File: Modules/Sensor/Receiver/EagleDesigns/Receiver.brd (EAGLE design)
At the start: 100 x 80 mm, 11 parts, among them U2 ATMEGA328P_TQFP

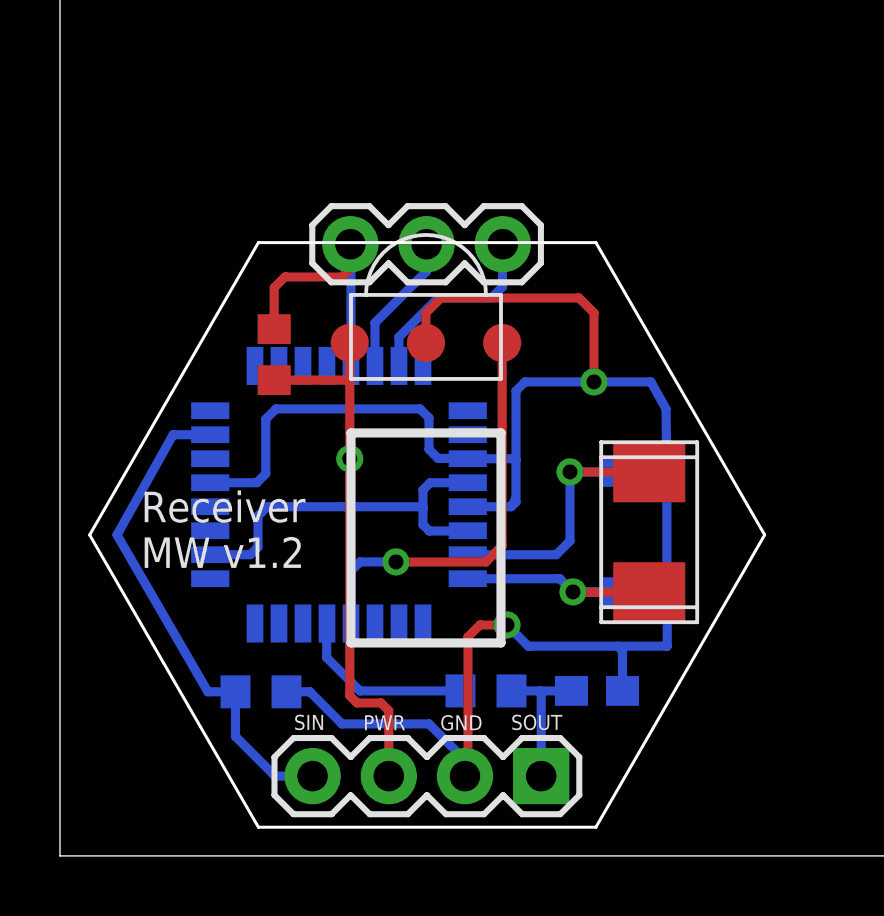
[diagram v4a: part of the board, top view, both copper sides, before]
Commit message: Receiver: removed crystal, modified to work with new bootloader #29
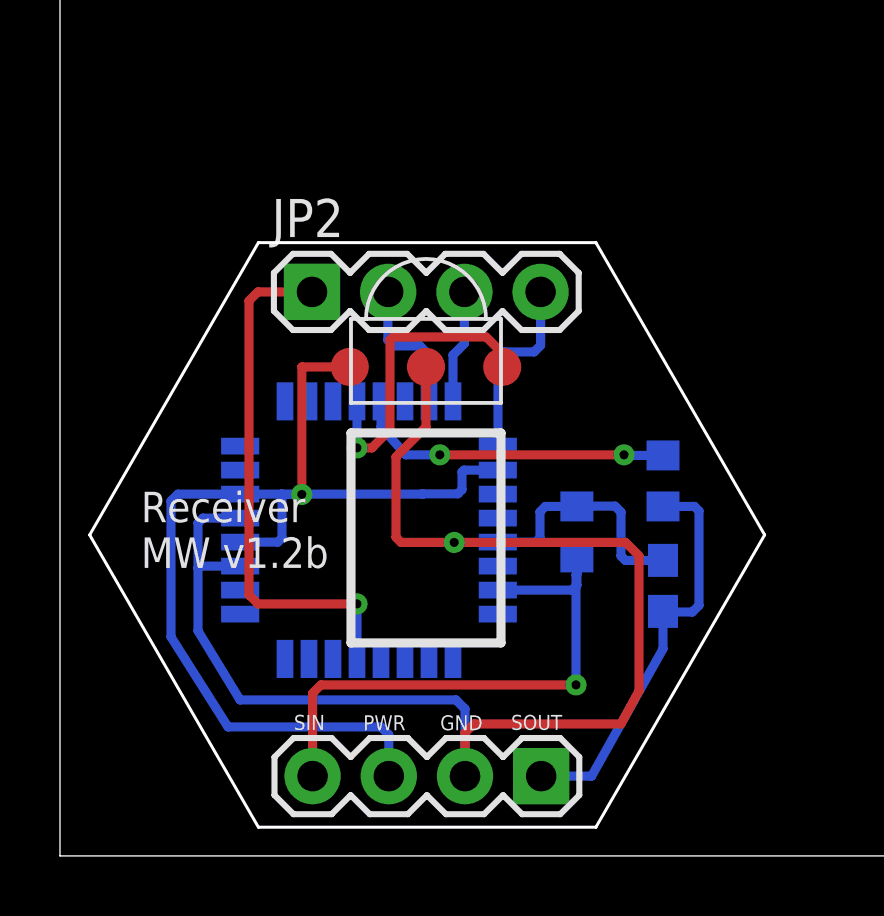
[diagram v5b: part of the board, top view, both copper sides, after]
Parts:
- removed C1, C2: 22pF, adafruit:C0603
- removed R2: 10K, resistor:R0603
- removed U$2: NX503, MakerWear:NX503
- JP2: device SparkFun-Connectors:1X03 -> SparkFun-Connectors:1X04
- moved R1 11.8 mm to (17.2, 10.8), turned to 270 degrees
- moved R4 9.15 mm to (20.1, 12.5), turned to 90 degrees
- moved C3 4.13 mm to (20.1, 9.00), turned to 90 degrees
- moved JP2 2.04 mm to (8.40, 18.8)
- moved U2 1.55 mm to (10.3, 10.9), turned to 180 degrees
- moved U$1 0.80 mm to (12.2, 17.9)
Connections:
- removed net N$1: C1.1, U$2.P$1, U2.7
- removed net N$3: C2.1, U$2.P$2, U2.8
- removed net RX: JP2.2, U2.30
- removed net TX: JP2.3, U2.31
- new net MISO: JP2.3, U2.16
- new net MOSI: JP2.2, U2.15
- new net SCK: JP2.4, U2.17
- net GND: no longer C1.2, C2.2
- net RESET: no longer R2.1
- net VCC: no longer R2.2
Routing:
- net N$1: track 10.1 -> 0.00 mm, vias 1 -> 0
- net 1X3SOUT: track 4.86 -> 13.5 mm
- net RESET: track 9.08 -> 17.6 mm, vias 0 -> 1
- net N$3: track 7.68 -> 0.00 mm, vias 1 -> 0
- net GND: track 62.9 -> 55.6 mm, vias 2 -> 1
- net TX: track 6.53 -> 0.00 mm
- net SCK: track 0.00 -> 6.32 mm
- net RX: track 4.77 -> 0.00 mm
- net MOSI: track 0.00 -> 4.73 mm
- net OUT: track 6.06 -> 10.7 mm, vias 0 -> 2
- net MISO: track 0.00 -> 3.80 mm
- net VCC: track 32.4 -> 36.1 mm
- net IR-IN: track 13.9 -> 10.4 mm
- net 1X3SIN: track 16.6 -> 19.0 mm, vias 0 -> 1
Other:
- board text added: "Receiver MW v1.2b"
- board text removed: "Receiver MW v1.2"
